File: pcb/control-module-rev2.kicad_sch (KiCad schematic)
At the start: 22 parts, among them J1 Screw_Terminal_01x06, J2 Conn_01x07_Pin, J5 Screw_Terminal_01x02, SW1 SW_DIP_x04, U1 TC2185-3.3VxCTTR

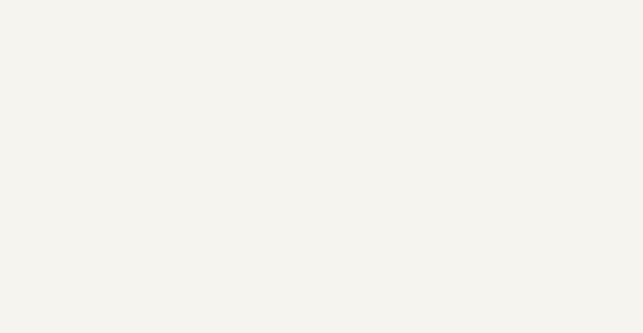
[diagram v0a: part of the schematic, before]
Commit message: Labeled max board dimensions in root sch
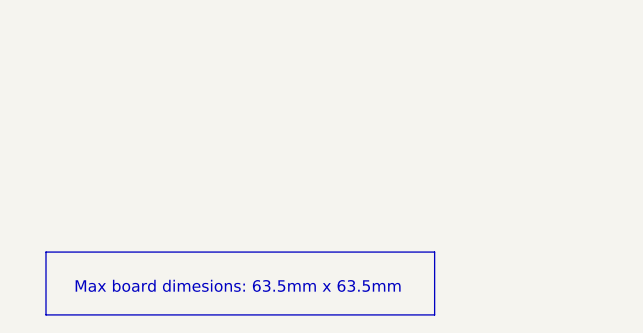
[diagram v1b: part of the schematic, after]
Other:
- note added: "Max board dimesions: 63.5mm x 63.5mm"
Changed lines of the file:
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@@
 	)
 	(rectangle
+		(start 21.59 190.5)
+		(end 64.77 197.485)
+		(stroke
+			(width 0)
+			(type default)
+		)
+		(fill
+			(type none)
+		)
+	)
+	(rectangle
 		(start 189.23 26.67)
 		(end 250.19 129.54)
@@
 		)
 	)
+	(text "Max board dimesions: 63.5mm x 63.5mm"
+		(exclude_from_sim no)
+		(at 42.926 194.564 0)
+		(effects
+			(font
+				(size 1.27 1.27)
+			)
+		)
+	)
 	(text "Divide battery voltage by four to\nfit in ADC range. Will by \nmultiplied by 4 in software."
 		(exclude_from_sim no)
@@
 		)
 		(instances
-			(project "control-module"
+			(project "control-module-rev2"
 				(path "/ba7b4294-8d75-4b9e-892f-fb52727887ec"
 					(page "5")
@@
 		)
 		(instances
-			(project "control-module"
+			(project "control-module-rev2"
 				(path "/ba7b4294-8d75-4b9e-892f-fb52727887ec"
 					(page "4")
@@
 		)
 		(instances
-			(project "control-module"
+			(project "control-module-rev2"
 				(path "/ba7b4294-8d75-4b9e-892f-fb52727887ec"
 					(page "7")
@@
 		)
 		(instances
-			(project "control-module"
+			(project "control-module-rev2"
 				(path "/ba7b4294-8d75-4b9e-892f-fb52727887ec"
 					(page "6")
@@
 		)
 		(instances
-			(project "control-module"
+			(project "control-module-rev2"
 				(path "/ba7b4294-8d75-4b9e-892f-fb52727887ec"
 					(page "3")
@@
 		)
 		(instances
-			(project "control-module"
+			(project "control-module-rev2"
 				(path "/ba7b4294-8d75-4b9e-892f-fb52727887ec"
 					(page "6")
@@
 		)
 		(instances
-			(project "control-module"
+			(project "control-module-rev2"
 				(path "/ba7b4294-8d75-4b9e-892f-fb52727887ec"
 					(page "2")
